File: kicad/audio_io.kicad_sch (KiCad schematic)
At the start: 16 parts, among them J3 PJ-603, J4 PJ-603, J5 PJ-328A0-B, J6 PJ-328A0-B, SW5 MSS22D18G2 125, U5 OPA1678

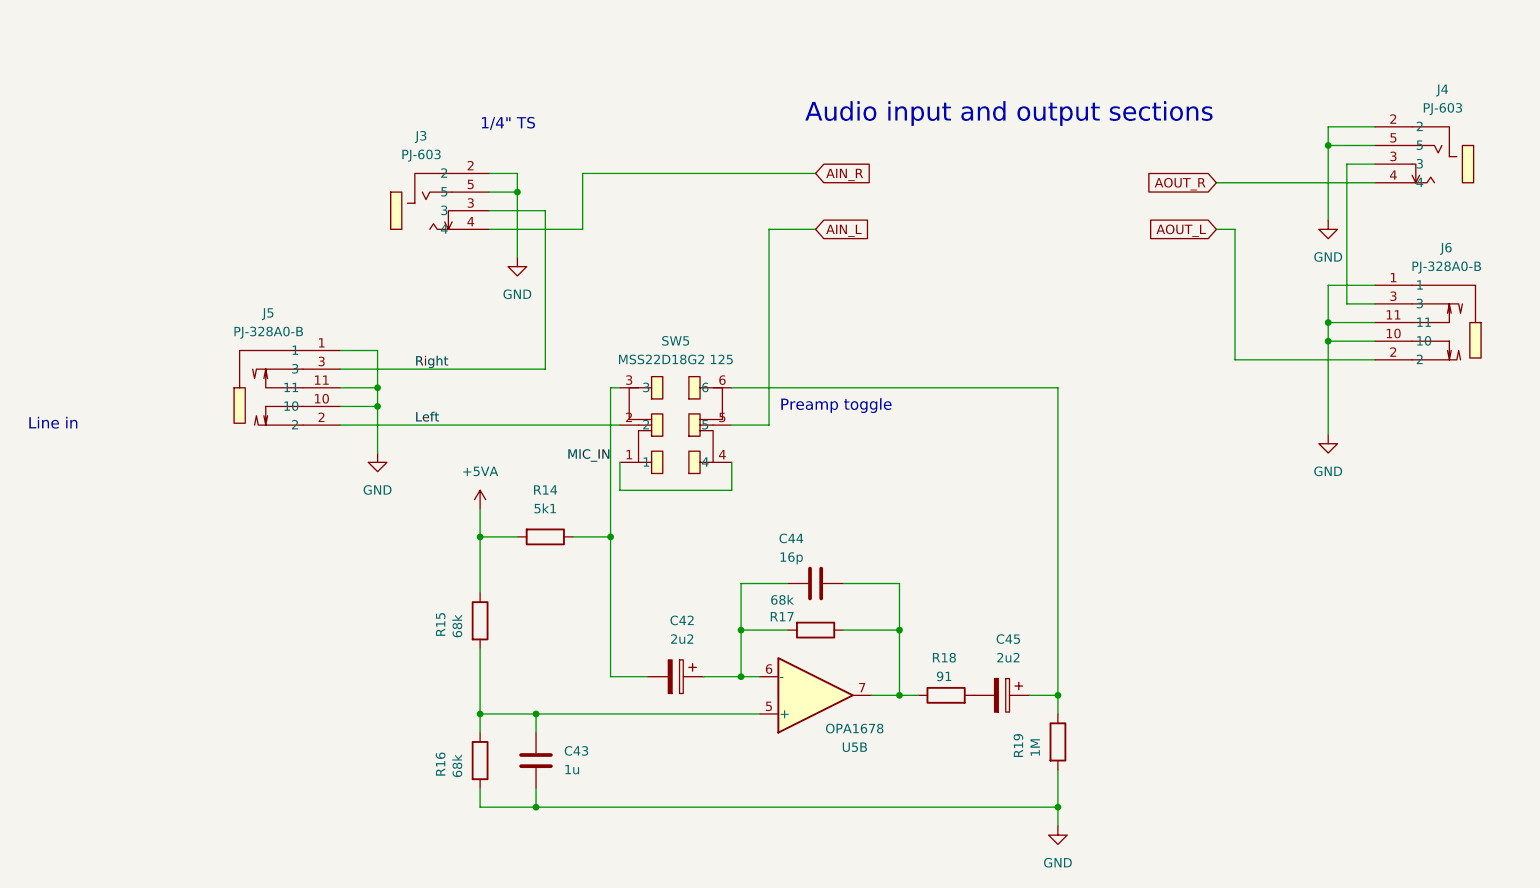
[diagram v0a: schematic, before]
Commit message: moved to hierarchical sheets
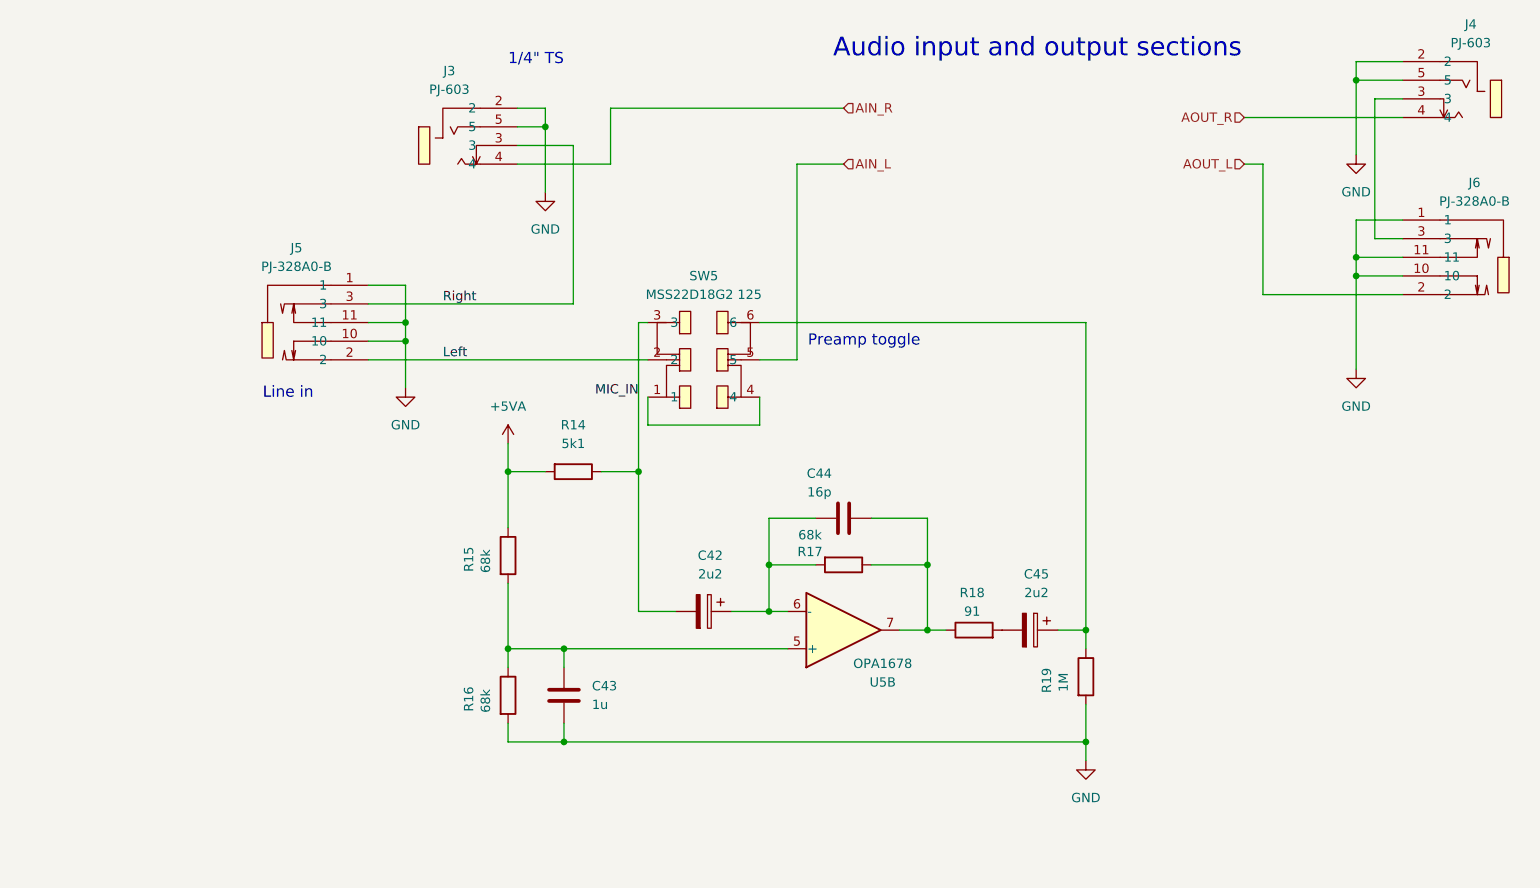
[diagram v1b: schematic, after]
